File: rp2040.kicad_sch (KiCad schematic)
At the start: 30 parts, among them J1 USB_C_Receptacle_USB2.0, SW1 SW_SPST, SW2 SW_SPST, U1 W25Q32JVSS, U2 AP1117-33, U3 RP2040, Y1 Crystal

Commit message: Footprint assignment
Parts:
- removed Y1: Crystal, symbol Device:Crystal
- added J2, J3: Conn_01x18, Connector_PinHeader_2.54mm:PinHeader_1x18_P2.54mm_Vertical, symbol Connector_Generic:Conn_01x18
- added Y1: 12MHz, Crystal:Crystal_SMD_2520-4Pin_2.5x2.0mm, symbol Device:Crystal_GND24
- C1, C10, C11, C12, C13, C14, C15, C16, C4, C5, C6, C7, C8, C9: footprint (none) -> Capacitor_SMD:C_0603_1608Metric_Pad1.08x0.95mm_HandSolder
- C2, C3: value 1uF -> 10uF; footprint (none) -> Capacitor_SMD:C_0603_1608Metric_Pad1.08x0.95mm_HandSolder
- J1: footprint (none) -> Connector_USB:USB_C_Receptacle_XKB_U262-16XN-4BVC11
- R1, R2, R3, R4, R5, R6, R7: footprint (none) -> Resistor_SMD:R_0603_1608Metric_Pad0.98x0.95mm_HandSolder
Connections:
- net +3V3: now also J3.3 (Pin_3)
- net GND: now also J2.1 (Pin_1), J2.18 (Pin_18), J3.1 (Pin_1), J3.18 (Pin_18), Y1.2, Y1.4
- net VBUS: now also J3.2 (Pin_2)
- net at C5.2, U3.21 (XOUT): now also Y1.1
- net at C4.2, U3.20 (XIN): now also Y1.3
- net GPIO8: now reaches U3.11 (GPIO8)
- net GPIO8: now also J2.10 (Pin_10)
- net GPIO9: now reaches U3.12 (GPIO9)
- net GPIO9: now also J2.11 (Pin_11)
- net GPIO10: now reaches U3.13 (GPIO10)
- net GPIO10: now also J2.12 (Pin_12)
- net GPIO11: now reaches U3.14 (GPIO11)
- net GPIO11: now also J2.13 (Pin_13)
- net GPIO12: now reaches U3.15 (GPIO12)
- net GPIO12: now also J2.14 (Pin_14)
- net GPIO13: now reaches U3.16 (GPIO13)
- net GPIO13: now also J2.15 (Pin_15)
- net GPIO14: now reaches U3.17 (GPIO14)
- net GPIO14: now also J2.16 (Pin_16)
- net GPIO15: now reaches U3.18 (GPIO15)
- net GPIO15: now also J2.17 (Pin_17)
- net GPIO0: now reaches U3.2 (GPIO0)
- net GPIO0: now also J2.2 (Pin_2)
- net GPIO16: now reaches U3.27 (GPIO16)
- net GPIO16: now also J3.4 (Pin_4)
- net GPIO17: now reaches U3.28 (GPIO17)
- net GPIO17: now also J3.5 (Pin_5)
- net GPIO18: now reaches U3.29 (GPIO18)
- net GPIO18: now also J3.6 (Pin_6)
- net GPIO1: now reaches U3.3 (GPIO1)
- net GPIO1: now also J2.3 (Pin_3)
- net GPIO19: now reaches U3.30 (GPIO19)
- net GPIO19: now also J3.7 (Pin_7)
- net GPIO20: now reaches U3.31 (GPIO20)
- net GPIO20: now also J3.8 (Pin_8)
- net GPIO21: now reaches U3.32 (GPIO21)
- net GPIO21: now also J3.9 (Pin_9)
- net GPIO22: now reaches U3.34 (GPIO22)
- net GPIO22: now also J3.10 (Pin_10)
- net GPIO23: now reaches U3.35 (GPIO23)
- net GPIO23: now also J3.11 (Pin_11)
- net GPIO24: now reaches U3.36 (GPIO24)
- net GPIO24: now also J3.12 (Pin_12)
- net GPIO25: now reaches U3.37 (GPIO25)
- net GPIO25: now also J3.13 (Pin_13)
- net GPIO26: now reaches U3.38 (GPIO26_ADC0)
- net GPIO26: now also J3.14 (Pin_14)
- net GPIO27: now reaches U3.39 (GPIO27_ADC1)
- net GPIO27: now also J3.15 (Pin_15)
- net GPIO2: now reaches U3.4 (GPIO2)
- net GPIO2: now also J2.4 (Pin_4)
- net GPIO28: now reaches U3.40 (GPIO28_ADC2)
- net GPIO28: now also J3.16 (Pin_16)
- net GPIO29: now reaches U3.41 (GPIO29_ADC3)
- net GPIO29: now also J3.17 (Pin_17)
- net GPIO3: now reaches U3.5 (GPIO3)
- net GPIO3: now also J2.5 (Pin_5)
- net GPIO4: now reaches U3.6 (GPIO4)
- net GPIO4: now also J2.6 (Pin_6)
- net GPIO5: now reaches U3.7 (GPIO5)
- net GPIO5: now also J2.7 (Pin_7)
- net GPIO6: now reaches U3.8 (GPIO6)
- net GPIO6: now also J2.8 (Pin_8)
- net GPIO7: now reaches U3.9 (GPIO7)
- net GPIO7: now also J2.9 (Pin_9)

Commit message: Routing finished
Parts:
- removed J2, J3: Conn_01x18, Connector_PinHeader_2.54mm:PinHeader_1x18_P2.54mm_Vertical, symbol Connector_Generic:Conn_01x18
- added J2, J3: Conn_02x10_Odd_Even, Connector_PinHeader_2.54mm:PinHeader_2x10_P2.54mm_Vertical, symbol Connector_Generic:Conn_02x10_Odd_Even
- added J4: Conn_01x08, footprints:SOIC_clipProgSmall, symbol Connector_Generic:Conn_01x08
- added R8: 1K, Resistor_SMD:R_0402_1005Metric_Pad0.72x0.64mm_HandSolder, symbol Device:R
- C1, C10, C11, C12, C13, C14, C15, C16, C4, C5, C6, C7, C8, C9: footprint Capacitor_SMD:C_0603_1608Metric_Pad1.08x0.95mm_HandSolder -> Capacitor_SMD:C_0402_1005Metric_Pad0.74x0.62mm_HandSolder
- R1, R2, R3, R4, R5, R6, R7: footprint Resistor_SMD:R_0603_1608Metric_Pad0.98x0.95mm_HandSolder -> Resistor_SMD:R_0402_1005Metric_Pad0.72x0.64mm_HandSolder
- U1: footprint Package_SO:SOIC-8_5.23x5.23mm_P1.27mm -> USON:SOIC-USON-8
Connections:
- net +3V3: now also J2.16 (Pin_16), J4.1 (Pin_1)
- net GND: now also J2.1 (Pin_1), J3.13 (Pin_13), J3.2 (Pin_2), J4.4 (Pin_4)
- net GPIO0: now also J3.1 (Pin_1), J4.2 (Pin_2)
- net GPIO1: now also J3.3 (Pin_3), J4.3 (Pin_3)
- net GPIO10: now also J2.13 (Pin_13)
- net GPIO11: now also J2.14 (Pin_14)
- net GPIO12: now also J2.15 (Pin_15)
- net GPIO13: now also J2.17 (Pin_17)
- net GPIO14: now also J2.18 (Pin_18)
- net GPIO15: now also J2.19 (Pin_19)
- net GPIO16: now also J3.19 (Pin_19)
- net GPIO17: now also J3.20 (Pin_20)
- net GPIO18: now also J3.17 (Pin_17)
- net GPIO19: now also J3.18 (Pin_18)
- net GPIO2: now also J2.5 (Pin_5)
- net GPIO20: now also J3.16 (Pin_16)
- net GPIO21: now also J3.14 (Pin_14)
- net GPIO22: now also J3.11 (Pin_11)
- net GPIO23: now also J3.12 (Pin_12)
- net GPIO24: now also J3.9 (Pin_9)
- net GPIO25: now also J3.10 (Pin_10)
- net GPIO26: now also J3.7 (Pin_7)
- net GPIO27: now also J3.8 (Pin_8)
- net GPIO28: now also J3.5 (Pin_5)
- net GPIO29: now also J3.6 (Pin_6)
- net GPIO3: now also J2.6 (Pin_6)
- net GPIO4: now also J2.7 (Pin_7)
- net GPIO5: now also J2.8 (Pin_8)
- net GPIO6: now also J2.9 (Pin_9)
- net GPIO7: now also J2.10 (Pin_10)
- net GPIO8: now also J2.11 (Pin_11)
- net GPIO9: now also J2.12 (Pin_12)
- net VBUS: now also J3.15 (Pin_15)
- net at C5.2, Y1.1: now also R8.1; no longer U3.21 (XOUT)
- net SWCLK: now reaches U3.24 (SWCLK)
- net SWCLK: now also J4.6 (Pin_6)
- net SWD: now reaches U3.25 (SWD)
- net SWD: now also J4.5 (Pin_5)
- net RUN: now reaches R5.2, SW2.2 (B), U3.26 (RUN)
- net RUN: now also J2.2 (Pin_2), J4.8 (Pin_8)
- new net: R8.2, U3.21 (XOUT)
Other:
- moved on the sheet: C4, C5, Y1

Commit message: Some random tweaks
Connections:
- net GND: now also U1.9 (GND)
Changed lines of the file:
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@@
-    (stroke (width 0) (type default) (color 0 0 0 0))
-  )
-  (wire (pts (xy 204.47 146.685) (xy 212.09 146.685))
     (stroke (width 0) (type default) (color 0 0 0 0))
   )
@@
     )
     (property "Datasheet" "" (id 3) (at 92.075 96.52 0)
-      (effects (font (size 1.27 1.27)) hide)
-    )
-    (pin "1")
-  )
-  (symbol (lib_id "power:+3V3") (at 59.055 150.495 0) (unit 1)
-    (in_bom yes) (on_board yes) (fields_autoplaced)
-    (property "Reference" "#PWR0140" (id 0) (at 59.055 154.305 0)
-      (effects (font (size 1.27 1.27)) hide)
-    )
-    (property "Value" "+3V3" (id 1) (at 59.055 145.415 0))
-    (property "Footprint" "" (id 2) (at 59.055 150.495 0)
-      (effects (font (size 1.27 1.27)) hide)
-    )
-    (property "Datasheet" "" (id 3) (at 59.055 150.495 0)
       (effects (font (size 1.27 1.27)) hide)
     )
@@
     (pin "3")
     (pin "4")
+    (pin "9")
     (pin "5")
     (pin "6")
@@
     (pin "8")
   )
-  (symbol (lib_id "power:GND") (at 204.47 146.685 270) (unit 1)
-    (in_bom yes) (on_board yes)
-    (property "Reference" "#PWR0137" (id 0) (at 198.12 146.685 0)
-      (effects (font (size 1.27 1.27)) hide)
-    )
-    (property "Value" "GND" (id 1) (at 198.12 146.685 90))
-    (property "Footprint" "" (id 2) (at 204.47 146.685 0)
-      (effects (font (size 1.27 1.27)) hide)
-    )
-    (property "Datasheet" "" (id 3) (at 204.47 146.685 0)
+  (symbol (lib_id "power:+3V3") (at 59.055 150.495 0) (unit 1)
+    (in_bom yes) (on_board yes) (fields_autoplaced)
+    (property "Reference" "#PWR0137" (id 0) (at 59.055 154.305 0)
+      (effects (font (size 1.27 1.27)) hide)
+    )
+    (property "Value" "+3V3" (id 1) (at 59.055 145.415 0))
+    (property "Footprint" "" (id 2) (at 59.055 150.495 0)
+      (effects (font (size 1.27 1.27)) hide)
+    )
+    (property "Datasheet" "" (id 3) (at 59.055 150.495 0)
       (effects (font (size 1.27 1.27)) hide)
     )
@@
       (reference "#PWR0136") (unit 1) (value "GND") (footprint "")
     )
-    (path "/ca1df078-a338-4f08-9b0f-17537815e1aa"
-      (reference "#PWR0137") (unit 1) (value "GND") (footprint "")
+    (path "/caaf039a-70b7-4438-bb89-b2e174d7561f"
+      (reference "#PWR0137") (unit 1) (value "+3V3") (footprint "")
     )
     (path "/8f47bff4-46fb-49f7-a73e-5939f2cfe4bf"
@@
       (reference "#PWR0139") (unit 1) (value "GND") (footprint "")
     )
-    (path "/1586e942-dabe-4e3c-9fb0-908f9a74ffa4"
-      (reference "#PWR0140") (unit 1) (value "+3V3") (footprint "")
-    )
     (path "/f4b7d2a5-c44b-4e17-9aa9-f6e397713786"

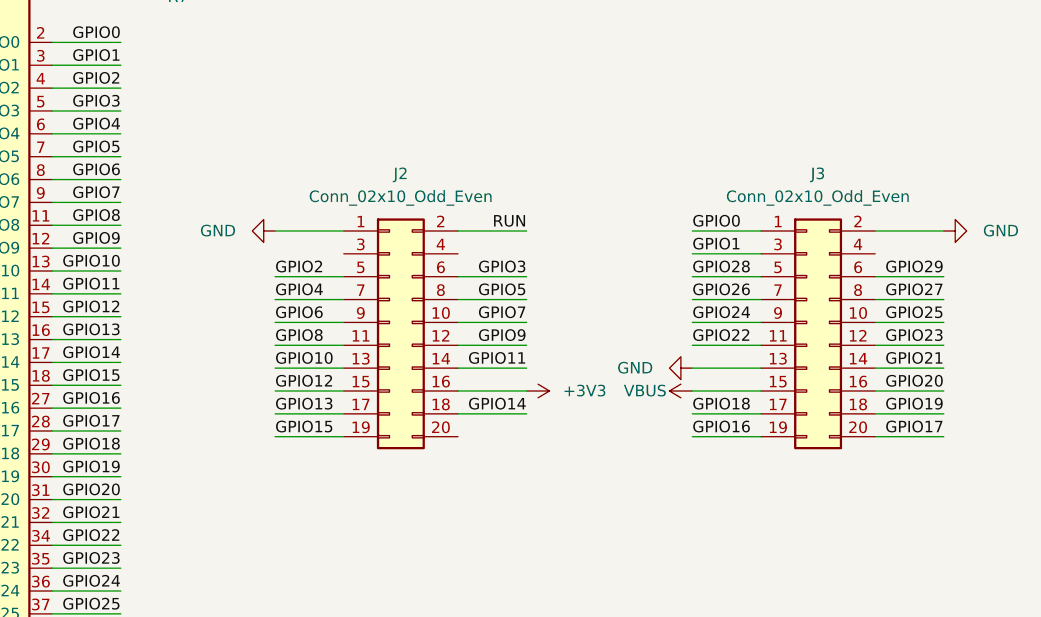
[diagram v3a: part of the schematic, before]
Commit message: Rearranged pinheaders, added logo and random tweaks
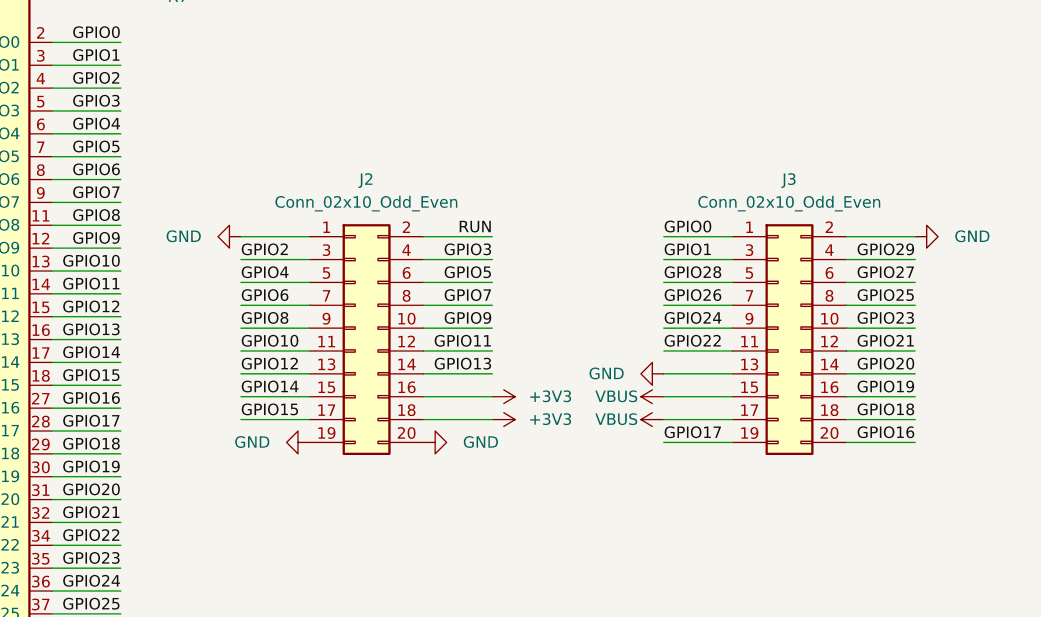
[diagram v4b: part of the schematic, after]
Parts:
- U2: footprint Package_TO_SOT_SMD:SOT-223-3_TabPin2 -> Package_TO_SOT_SMD:SOT-89-3
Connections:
- net +3V3: now also J2.18 (Pin_18)
- net GND: now also J2.19 (Pin_19), J2.20 (Pin_20)
- net GPIO10: now also J2.11 (Pin_11); no longer J2.13 (Pin_13)
- net GPIO11: now also J2.12 (Pin_12); no longer J2.14 (Pin_14)
- net GPIO12: now also J2.13 (Pin_13); no longer J2.15 (Pin_15)
- net GPIO13: now also J2.14 (Pin_14); no longer J2.17 (Pin_17)
- net GPIO14: now also J2.15 (Pin_15); no longer J2.18 (Pin_18)
- net GPIO15: now also J2.17 (Pin_17); no longer J2.19 (Pin_19)
- net GPIO16: now also J3.20 (Pin_20); no longer J3.19 (Pin_19)
- net GPIO17: now also J3.19 (Pin_19); no longer J3.20 (Pin_20)
- net GPIO18: now also J3.18 (Pin_18); no longer J3.17 (Pin_17)
- net GPIO19: now also J3.16 (Pin_16); no longer J3.18 (Pin_18)
- net GPIO2: now also J2.3 (Pin_3); no longer J2.5 (Pin_5)
- net GPIO20: now also J3.14 (Pin_14); no longer J3.16 (Pin_16)
- net GPIO21: now also J3.12 (Pin_12); no longer J3.14 (Pin_14)
- net GPIO23: now also J3.10 (Pin_10); no longer J3.12 (Pin_12)
- net GPIO25: now also J3.8 (Pin_8); no longer J3.10 (Pin_10)
- net GPIO27: now also J3.6 (Pin_6); no longer J3.8 (Pin_8)
- net GPIO29: now also J3.4 (Pin_4); no longer J3.6 (Pin_6)
- net GPIO3: now also J2.4 (Pin_4); no longer J2.6 (Pin_6)
- net GPIO4: now also J2.5 (Pin_5); no longer J2.7 (Pin_7)
- net GPIO5: now also J2.6 (Pin_6); no longer J2.8 (Pin_8)
- net GPIO6: now also J2.7 (Pin_7); no longer J2.9 (Pin_9)
- net GPIO7: now also J2.8 (Pin_8); no longer J2.10 (Pin_10)
- net GPIO8: now also J2.9 (Pin_9); no longer J2.11 (Pin_11)
- net GPIO9: now also J2.10 (Pin_10); no longer J2.12 (Pin_12)
- net VBUS: now also J3.17 (Pin_17)
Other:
- moved on the sheet: J2, J3
